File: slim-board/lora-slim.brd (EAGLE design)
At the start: 16.6 x 72.9 mm, 27 parts, among them IC1 STM32F030F4, IC2 ADP1607, J1 SWD_PTH_SHROUD, X1 SMA-142-0701-801/806, X2 UBLOX_MAX, X3 RFM98

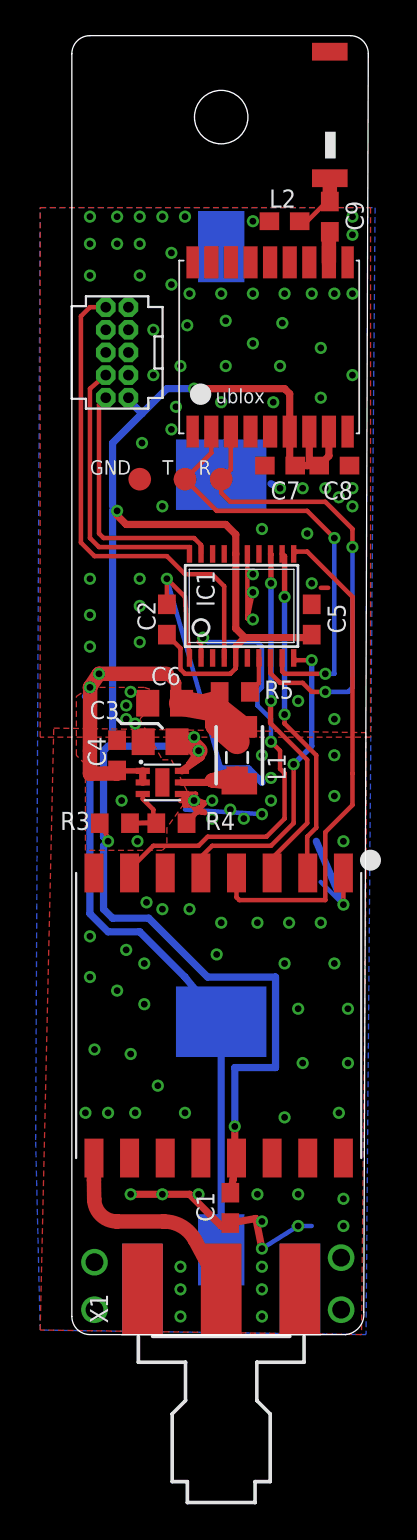
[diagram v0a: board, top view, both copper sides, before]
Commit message: Update slim-lora board. [inverted battery, remove gps rf parts, rework reg layout, add gpio1 header]
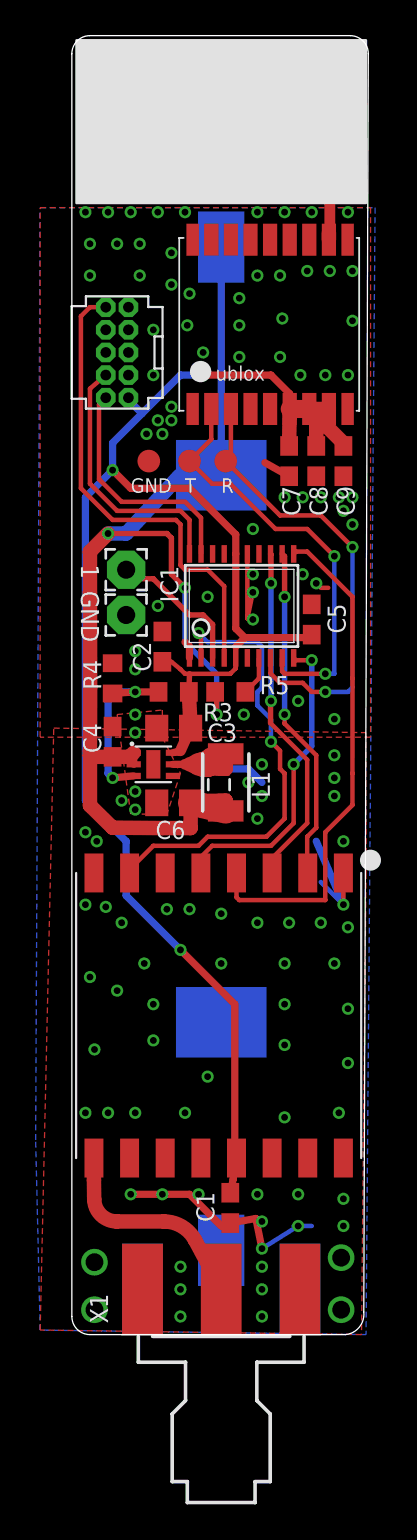
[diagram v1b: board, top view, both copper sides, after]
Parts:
- removed L2: (no value), SparkFun-Passives:0603
- added PAD1, PAD2: (no value), wirepad:2,15/1,0
- C9: value (none) -> 100p
- moved C9 13.7 mm to (19.1, 49.8)
- moved R4 8.77 mm to (6.10, 37.6), turned to 270 degrees
- moved R3 8.07 mm to (9.53, 36.8), turned to 0 degrees
- moved C6 5.61 mm to (9.53, 30.6)
- moved L1 1.83 mm to (12.1, 31.6), turned to 90 degrees
- moved L3 1.70 mm to (12.4, 31.8), turned to 90 degrees
- moved C2 1.55 mm to (8.89, 39.4)
- moved X2 1.27 mm to (15.0, 57.7)
- moved U$6 1.27 mm to (12.2, 33.0), turned to 270 degrees
- moved IC2 1.14 mm to (8.38, 32.8)
- moved TP1 1.14 mm to (8.13, 49.8)
- moved C3 1.08 mm to (9.53, 34.8)
- moved C8 1.05 mm to (17.5, 49.8), turned to 270 degrees
- moved TP2 1.05 mm to (10.4, 49.8)
- moved TP3 1.05 mm to (12.4, 49.8)
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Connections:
- removed net N$4: C9.1, L2.1, U$5.FEED
- net +3V3: now also C9.1
- net GND: now also C9.2, PAD1.1; no longer L2.2
- net GPIO1: now also PAD2.1
- net N$1: now also U$5.FEED; no longer C9.2
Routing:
- net GND: track 59.3 -> 31.1 mm, vias 129 -> 126
- net +3V3: track 111.7 -> 99.4 mm, vias 6 -> 3
- net GPIO1: track 0.00 -> 8.00 mm
- net N$6: track 4.63 -> 9.93 mm, vias 0 -> 2
- net VBAT: track 62.2 -> 66.0 mm, vias 2 -> 3
- net N$4: track 3.46 -> 0.00 mm
- net N$3: track 6.14 -> 3.52 mm
- net N$1: track 1.73 -> 3.50 mm
- net SWCLK: track 15.7 -> 14.8 mm
- net SWDAT: track 14.4 -> 13.5 mm
- net UART_RX: track 24.9 -> 24.1 mm
- net UART_TX: track 26.8 -> 26.0 mm
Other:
- board text added: "(c)"
- board text added: "1"
- board text added: "March 18"
- board text removed: "Sept 14"
- board text removed: "©"

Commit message: slim-board: Tweak cap values.
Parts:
- C9: value 100p -> 10n
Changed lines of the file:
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@@
 </element>
 <element name="U$1" library="Mine" package="SUSF-XSM" value="" x="19.05" y="30.48" rot="MR0"/>
-<element name="C9" library="rcl" package="C0603" value="100p" x="19.05" y="49.784" smashed="yes" rot="R270">
+<element name="C9" library="rcl" package="C0603" value="10n" x="19.05" y="49.784" smashed="yes" rot="R270">
 <attribute name="NAME" x="18.669" y="48.387" size="1.016" layer="25" font="vector" ratio="13" rot="R270"/>
 </element>
